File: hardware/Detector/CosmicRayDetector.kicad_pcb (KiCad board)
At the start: 2 copper layers, 100 x 100 mm, 110 parts, among them J1 USB_B_Micro, J10 Conn_02x04_Odd_Even, J11 Conn_02x02_Odd_Even, J12 Conn_02x04_Odd_Even, J13 Conn_02x02_Odd_Even, J14 Conn_02x02_Odd_Even, J15 Conn_02x02_Odd_Even, J16 Conn_02x02_Odd_Even, J17 Conn_02x02_Odd_Even, J18 Conn_02x02_Odd_Even, J2 Conn_02x02_Odd_Even, J3 Conn_02x02_Odd_Even, J4 Conn_02x02_Odd_Even, J5 Conn_02x04_Odd_Even, J51 Conn_02x05_Counter_Clockwise, J52 Conn_01x04, J6 Conn_02x04_Odd_Even, J7 Conn_02x04_Odd_Even, J8 Conn_02x04_Odd_Even, J9 Conn_02x04_Odd_Even, Q31 BC859, Q32 Q_NMOS_GDS, U1 STM32F030K6Tx, U2 HEF4093B, U3 LCD_I2C, U31 MC34063AD

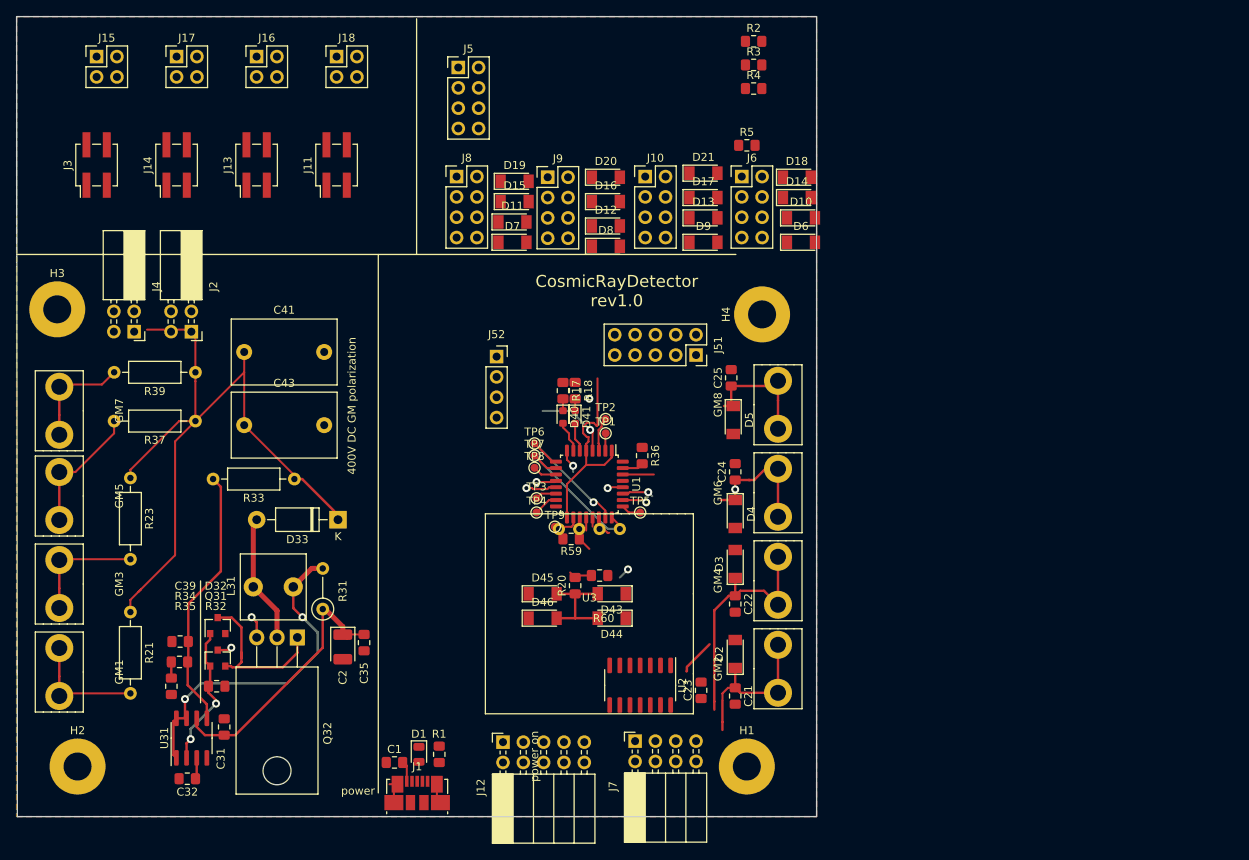
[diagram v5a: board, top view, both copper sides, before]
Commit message: removed parts not needed due to fpga use
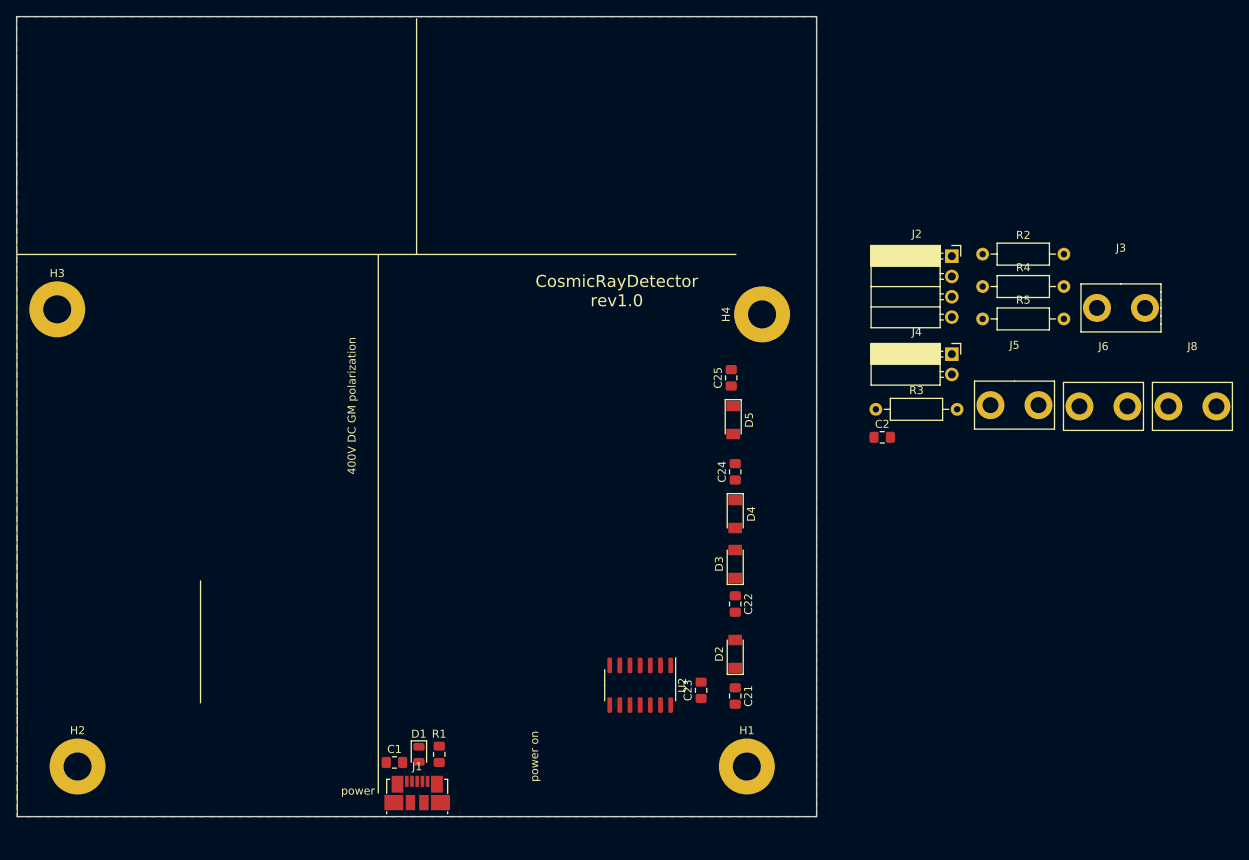
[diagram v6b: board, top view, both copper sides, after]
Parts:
- removed C31, C35: 100n, Capacitor_SMD:C_0805_2012Metric_Pad1.15x1.40mm_HandSolder
- removed C32: 3n2, Capacitor_SMD:C_0805_2012Metric_Pad1.15x1.40mm_HandSolder
- removed C39: 10n, Capacitor_SMD:C_0805_2012Metric_Pad1.15x1.40mm_HandSolder
- removed C41, C43: 10n/600V, Capacitor_THT:C_Rect_L13.0mm_W8.0mm_P10.00mm_FKS3_FKP3_MKS4
- removed D10, D11, D12, D13, D14, D15, D16, D17, D18, D19, D20, D21, D43, D44, D45, D46, D6, D7, D8, D9: 1n148, Diode_SMD:D_MiniMELF
- removed D32: D_Schottky, Diode_SMD:D_SOT-23_ANK
- removed D33: 1N4007, Diode_THT:D_DO-41_SOD81_P10.16mm_Horizontal
- removed D40, D41: LED, LED_SMD:LED_0603_1608Metric
- removed GM1, GM3, GM5, GM7: GM+, CosmicRayDetector:GeigerTube
- removed GM2, GM4, GM6, GM8: GM-, CosmicRayDetector:GeigerTube
- removed J10, J9: Conn_02x04_Odd_Even, Connector_PinHeader_2.54mm:PinHeader_2x04_P2.54mm_Vertical
- removed J11, J13, J14: Conn_02x02_Odd_Even, Connector_PinHeader_2.54mm:PinHeader_2x02_P2.54mm_Vertical_SMD
- removed J12: Conn_02x04_Odd_Even, Connector_PinSocket_2.54mm:PinSocket_2x05_P2.54mm_Horizontal
- removed J15, J16, J17, J18: Conn_02x02_Odd_Even, Connector_PinHeader_2.54mm:PinHeader_2x02_P2.54mm_Vertical
- removed J51: Conn_02x05_Counter_Clockwise, Connector_PinSocket_2.54mm:PinSocket_2x05_P2.54mm_Vertical
- removed J52: Conn_01x04, Connector_PinSocket_2.54mm:PinSocket_1x04_P2.54mm_Vertical
- removed J7: Conn_02x04_Odd_Even, Connector_PinSocket_2.54mm:PinSocket_2x04_P2.54mm_Horizontal
- removed L31: 680m, Inductor_THT:L_Radial_L8.0mm_W8.0mm_P5.00mm_Neosid_NE-CPB-07E
- removed Q31: BC859, Package_TO_SOT_SMD:SOT-23
- removed Q32: Q_NMOS_GDS, Package_TO_SOT_THT:TO-220-3_Horizontal_TabDown
- removed R17, R18: 680R, Resistor_SMD:R_0805_2012Metric_Pad1.15x1.40mm_HandSolder
- removed R20: R, Resistor_SMD:R_0805_2012Metric_Pad1.15x1.40mm_HandSolder
- removed R21, R23, R37, R39: R, Resistor_THT:R_Axial_DIN0207_L6.3mm_D2.5mm_P10.16mm_Horizontal
- removed R31: R22/0.5W, Resistor_THT:R_Axial_DIN0207_L6.3mm_D2.5mm_P5.08mm_Vertical
- removed R32: 10k, Resistor_SMD:R_0805_2012Metric_Pad1.15x1.40mm_HandSolder
- removed R33: 10M, Resistor_THT:R_Axial_DIN0207_L6.3mm_D2.5mm_P10.16mm_Horizontal
- removed R34: 1k, Resistor_SMD:R_0805_2012Metric_Pad1.15x1.40mm_HandSolder
- removed R35: 30k, Resistor_SMD:R_0805_2012Metric_Pad1.15x1.40mm_HandSolder
- removed R36: 100k, Resistor_SMD:R_0805_2012Metric_Pad1.15x1.40mm_HandSolder
- removed R59, R60: 2k2, Resistor_SMD:R_0805_2012Metric_Pad1.15x1.40mm_HandSolder
- removed TP1, TP2, TP3, TP4, TP5, TP6, TP7, TP8, TP9: TestPoint, TestPoint:TestPoint_Pad_D1.0mm
- removed U1: STM32F030K6Tx, Package_QFP:LQFP-32_7x7mm_P0.8mm
- removed U3: LCD_I2C, CosmicRayDetector:LCD_I2C
- removed U31: MC34063AD, Package_SO:SOIC-8_3.9x4.9mm_P1.27mm
- C2: value 100u/6V3 -> 100n; footprint Capacitor_Tantalum_SMD:CP_EIA-3528-21_Kemet-B -> Capacitor_SMD:C_0805_2012Metric_Pad1.15x1.40mm_HandSolder
- J2: value Conn_02x02_Odd_Even -> Conn_01x04; footprint Connector_PinSocket_2.54mm:PinSocket_2x02_P2.54mm_Horizontal -> Connector_PinSocket_2.54mm:PinSocket_1x04_P2.54mm_Horizontal
- J3: value Conn_02x02_Odd_Even -> Conn_01x01_Female; footprint Connector_PinHeader_2.54mm:PinHeader_2x02_P2.54mm_Vertical_SMD -> CosmicRayDetector:GeigerTube
- J4: value Conn_02x02_Odd_Even -> Conn_01x02; footprint Connector_PinSocket_2.54mm:PinSocket_2x02_P2.54mm_Horizontal -> Connector_PinSocket_2.54mm:PinSocket_1x02_P2.54mm_Horizontal
- J5, J6, J8: value Conn_02x04_Odd_Even -> Conn_01x01_Female; footprint Connector_PinHeader_2.54mm:PinHeader_2x04_P2.54mm_Vertical -> CosmicRayDetector:GeigerTube
- R2, R3, R4, R5: value 680R -> R; footprint Resistor_SMD:R_0805_2012Metric_Pad1.15x1.40mm_HandSolder -> Resistor_THT:R_Axial_DIN0207_L6.3mm_D2.5mm_P10.16mm_Horizontal
- moved J3 128.4 mm to (138.0, 13.4), turned to 0 degrees
- moved J4 102.2 mm to (116.9, 27.2), turned to 0 degrees
- moved J2 95.5 mm to (116.9, 14.9), turned to 0 degrees
- moved J8 94.3 mm to (147.0, 25.7)
- moved J5 77.5 mm to (124.7, 25.6)
- moved C2 72.3 mm to (108.2, 37.6), turned to 0 degrees
- moved J6 49.7 mm to (135.9, 25.7)
- moved R3 45.7 mm to (107.4, 34.1)
- moved R2 39.1 mm to (120.8, 14.7)
- moved R4 37.8 mm to (120.8, 18.7)
- moved R5 36.6 mm to (120.8, 22.8)
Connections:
- J2 pad 1: GM_LAMP_POLARIZATION -> GM1
- J2 pad 2: GM_LAMP_POLARIZATION -> GM2
- J2 pad 3: GM_LAMP_POLARIZATION -> GM3
- J2 pad 4: GM_LAMP_POLARIZATION -> GM4
- J3 pad 1: GM_LAMP_POLARIZATION -> Net-(C21-Pad1)
- J4 pad 1: GND -> VCC_5V
- J5 pad 1: COL0 -> Net-(C22-Pad1)
- J6 pad 1: GND -> Net-(C24-Pad1)
- J8 pad 1: GND -> Net-(C25-Pad1)
- R2 pad 1: /BoardConnector/COL0_LOCAL -> Net-(C21-Pad1)
- R2 pad 2: VCC_5V -> GND
- R3 pad 1: /BoardConnector/COL1_LOCAL -> Net-(C22-Pad1)
- R3 pad 2: VCC_5V -> GND
- R4 pad 1: /BoardConnector/COL2_LOCAL -> Net-(C24-Pad1)
- R4 pad 2: VCC_5V -> GND
- R5 pad 1: /BoardConnector/COL3_LOCAL -> Net-(C25-Pad1)
- R5 pad 2: VCC_5V -> GND
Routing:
- net GM_LAMP_POLARIZATION: track 91.5 -> 0.00 mm
- net VCC_5V: track 65.3 -> 0.00 mm
- net Net-(L31-Pad1): track 42.1 -> 0.00 mm, vias 2 -> 0
- net Net-(C39-Pad1): track 33.0 -> 0.00 mm
- net Net-(C22-Pad1): track 30.3 -> 0.00 mm
- net Net-(D32-Pad1): track 21.1 -> 0.00 mm
- net Net-(C24-Pad1): track 21.0 -> 0.00 mm, vias 1 -> 0
- net Net-(C21-Pad1): track 20.0 -> 0.00 mm
- net Net-(D32-Pad2): track 18.1 -> 0.00 mm, vias 2 -> 0
- net Net-(GM5-Pad1): track 16.4 -> 0.00 mm
- net /DataAcquisition/SWCLK: track 16.3 -> 0.00 mm, vias 1 -> 0
- net Net-(D33-Pad2): track 16.1 -> 0.00 mm
- net Net-(C25-Pad1): track 15.4 -> 0.00 mm
- net Net-(GM1-Pad1): track 15.0 -> 0.00 mm
- net Net-(GM3-Pad1): track 14.9 -> 0.00 mm
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
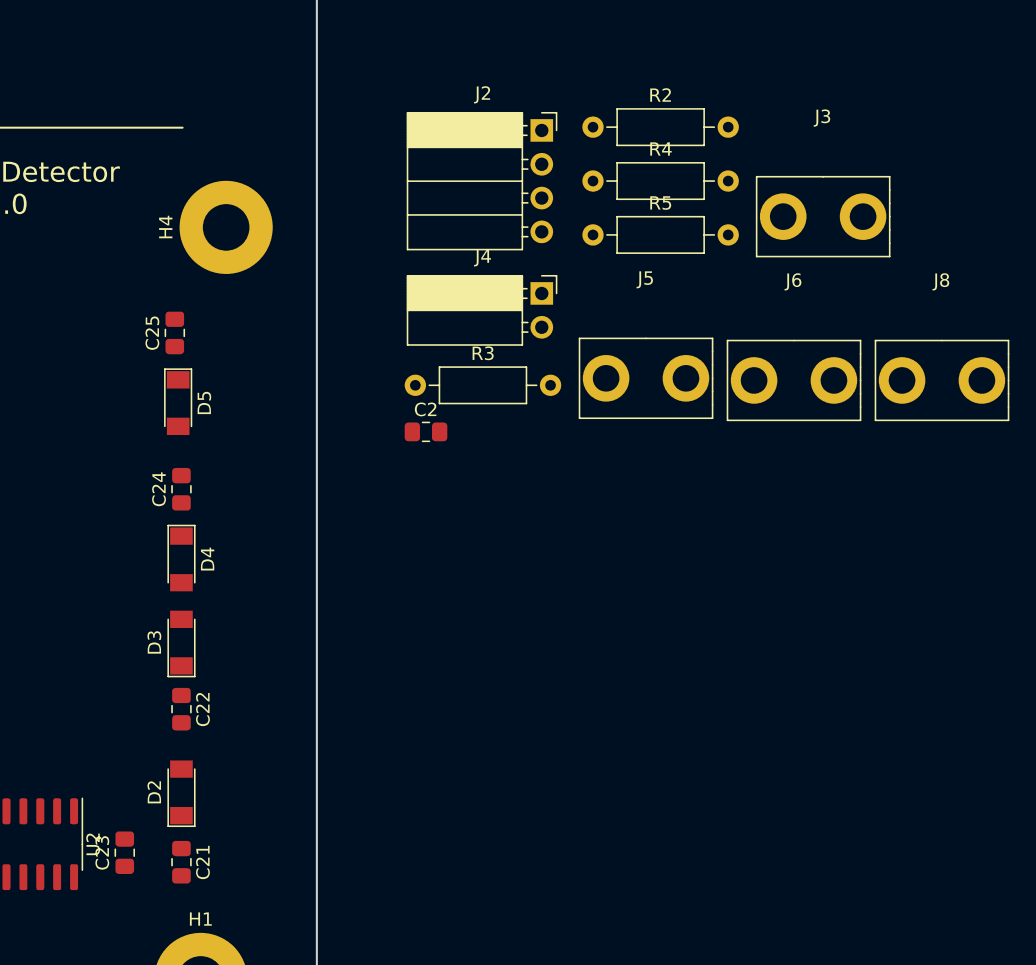
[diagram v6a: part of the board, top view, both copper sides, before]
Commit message: sheets updated to current design
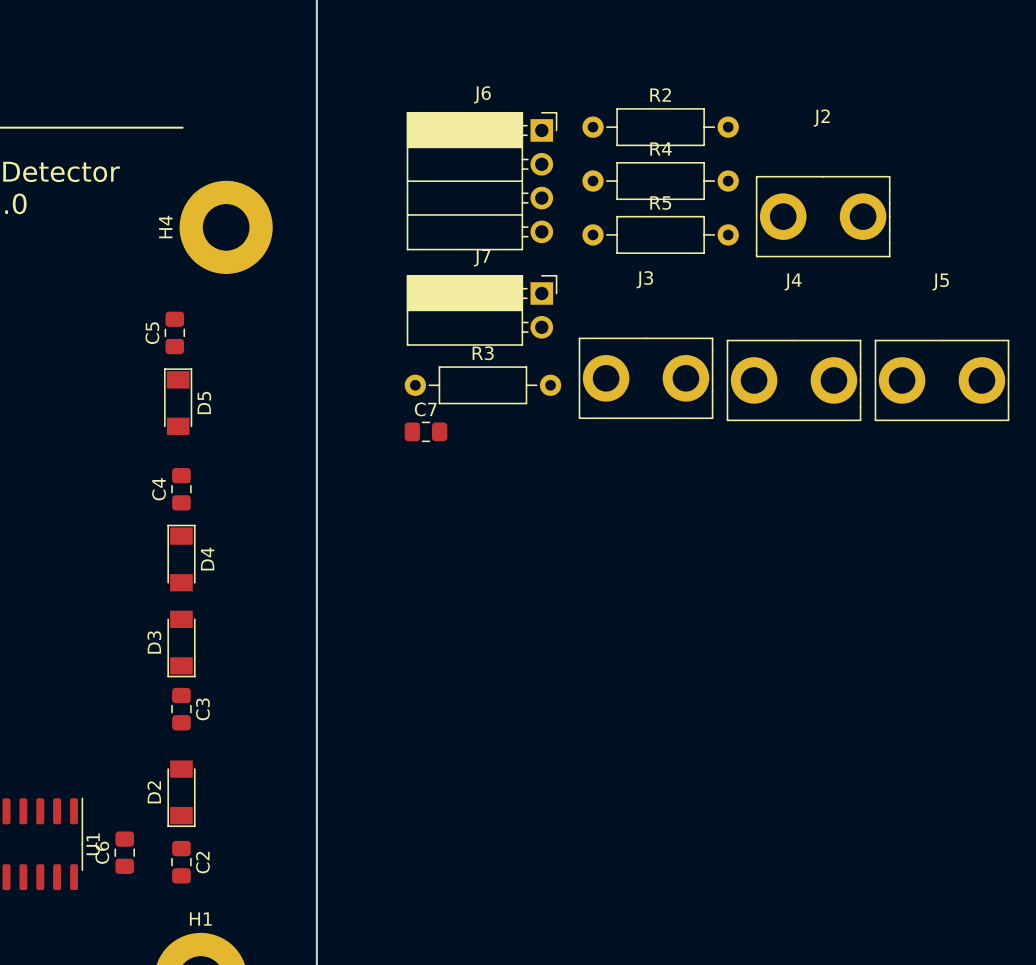
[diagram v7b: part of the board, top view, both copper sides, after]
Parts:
- renumbered C21 to C2, C22 to C3, C24 to C4, C25 to C5, C23 to C6, C2 to C7, J3 to J2, J5 to J3, J6 to J4, J8 to J5, J2 to J6, J4 to J7, U2 to U1
